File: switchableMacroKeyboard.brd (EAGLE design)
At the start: 58.4 x 114.3 mm, 40 parts

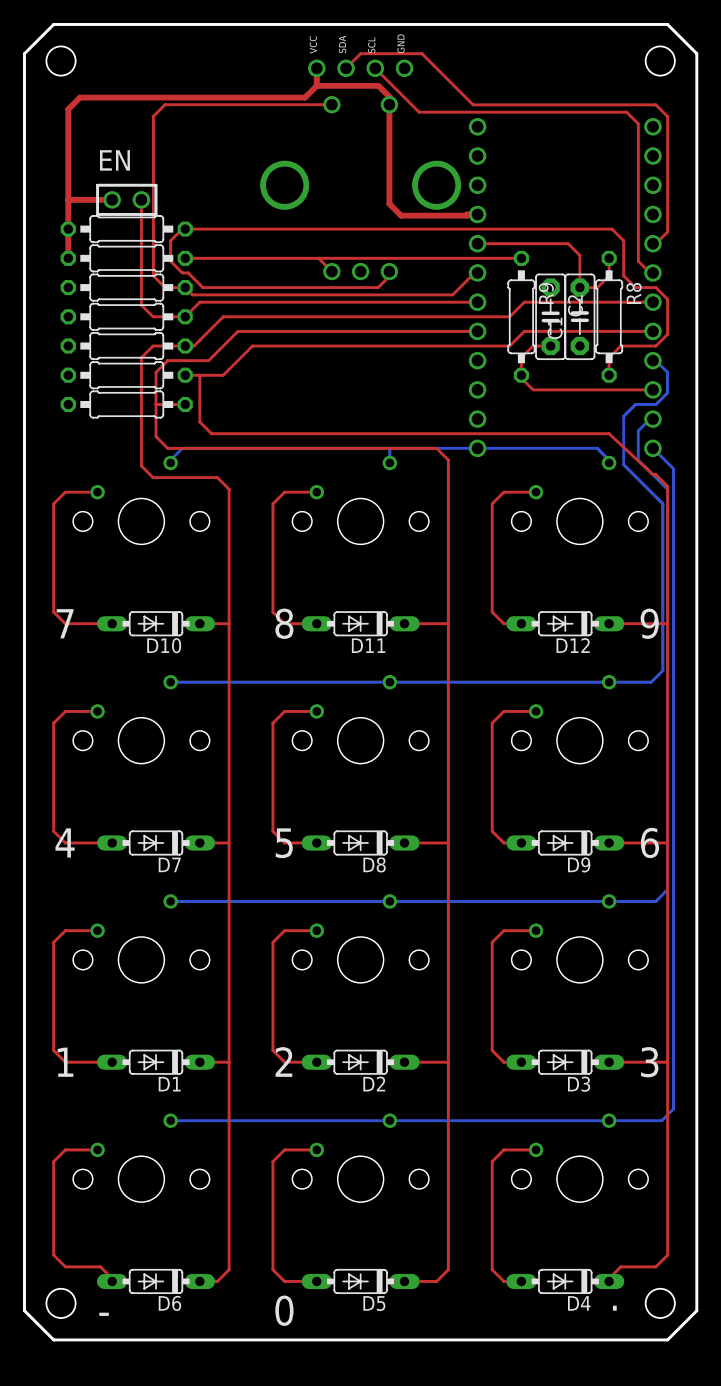
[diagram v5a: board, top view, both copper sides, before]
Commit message: Moved the Pro Micro board up to reduce interference with the key switches. Adjusted routing accordingly. Ordered this version in green.
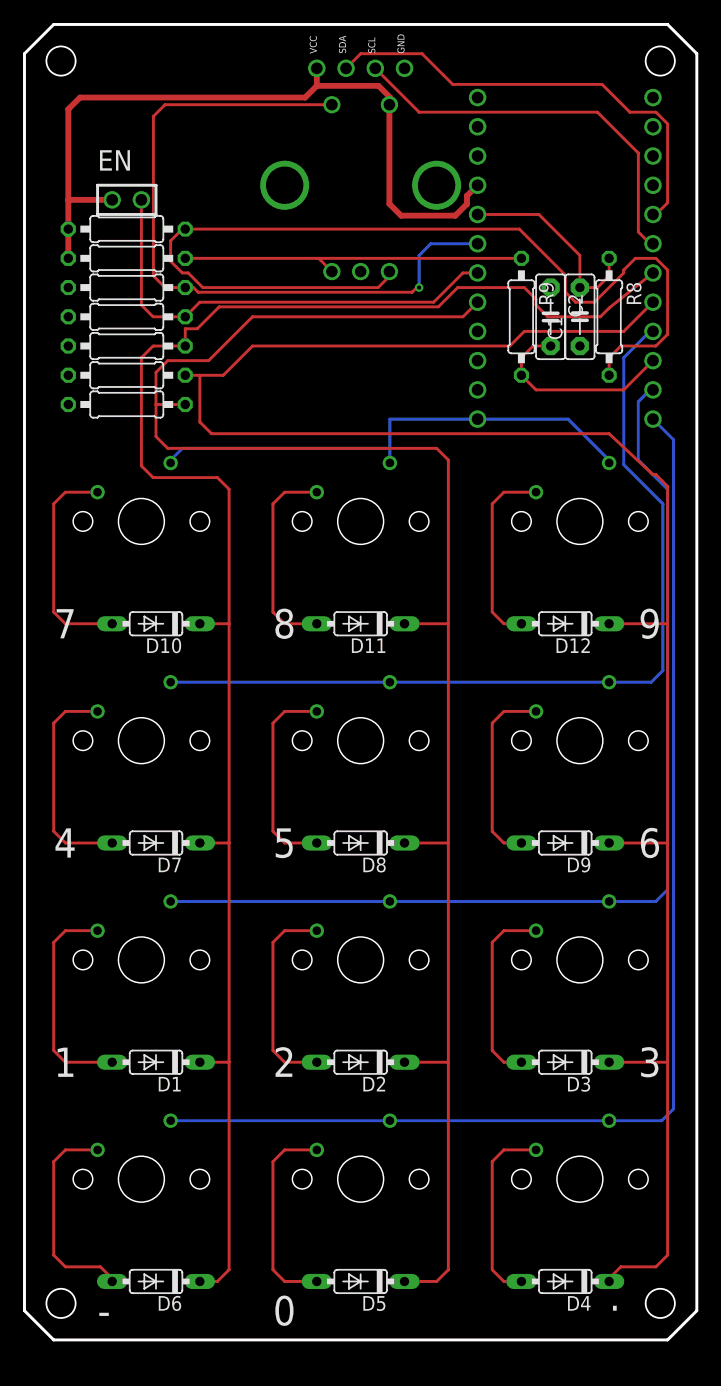
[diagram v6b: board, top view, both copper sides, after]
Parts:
- moved B1 2.54 mm to (47.0, 95.2)
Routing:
- net COL0: track 142.7 -> 146.8 mm
- net SCL: track 38.5 -> 34.5 mm
- net N$2: track 81.0 -> 84.9 mm
- net ROW0: track 40.7 -> 44.3 mm
- net SDA: track 42.5 -> 39.5 mm
- net ROW3: track 102.2 -> 104.8 mm
- net ROW2: track 86.2 -> 88.8 mm
- net SW-SIG: track 59.5 -> 61.9 mm, vias 0 -> 1
- net VCC: track 65.0 -> 66.4 mm
- net N$9: track 16.6 -> 17.6 mm
- net COL2: track 177.4 -> 178.4 mm
- net COL1: track 149.8 -> 150.9 mm
- net EN: track 39.3 -> 40.4 mm
- net N$1: track 16.6 -> 17.5 mm
